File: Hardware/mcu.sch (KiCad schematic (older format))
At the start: 45 parts, among them J3 SWD_programming, J4 Capsense_0, J5 Capsense_1, J6 Capsense_2, J7 Capsense_3, U7 CY8C4246AZI-L445, Y1 Crystal

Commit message: add Cmod cap to microcontroller for capsense operation.
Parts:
- added C?: 2.2nF, symbol C_Small
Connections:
- wire segments 98 -> 79
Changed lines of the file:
@@
 	1050 7350 1350 7350
 Wire Wire Line
-	1850 2150 2050 2150
-Wire Wire Line
-	2050 2150 2150 2150
+	1850 2150 2150 2150
 Wire Wire Line
 	1850 2250 2150 2250
@@
 	2150 2350 1850 2350
 Wire Wire Line
-	1500 4400 1500 4500
-Wire Wire Line
-	1500 4500 1500 4800
-Wire Wire Line
-	1500 4800 1500 4850
+	1500 4400 1500 4850
 Wire Wire Line
 	1500 4400 2150 4400
 Wire Wire Line
-	2000 4500 2000 4800
-Wire Wire Line
-	2000 4800 2000 4850
-Wire Wire Line
-	1900 4500 2000 4500
-Wire Wire Line
-	2000 4500 2150 4500
+	2000 4500 2000 4850
+Wire Wire Line
+	1900 4500 2150 4500
 Connection ~ 2000 4500
 Wire Wire Line
@@
 	2100 3950 2150 3950
 Wire Wire Line
-	1700 3050 1800 3050
-Wire Wire Line
-	1800 3050 1900 3050
-Wire Wire Line
-	1900 3050 2000 3050
+	1700 3050 2000 3050
 Connection ~ 1800 3050
 Wire Wire Line
-	1700 3250 1800 3250
-Wire Wire Line
-	1800 3250 1900 3250
-Wire Wire Line
-	1900 3250 2150 3250
+	1700 3250 2150 3250
 Connection ~ 1800 3250
 $Comp
@@
 $EndComp
 Wire Wire Line
-	1700 4100 1800 4100
-Wire Wire Line
-	1800 4100 1900 4100
-Wire Wire Line
-	1900 4100 2000 4100
+	1700 4100 2000 4100
 Connection ~ 1800 4100
 Wire Wire Line
-	1700 3900 1800 3900
-Wire Wire Line
-	1800 3900 1900 3900
-Wire Wire Line
-	1900 3900 1950 3900
+	1700 3900 1950 3900
 Connection ~ 1800 3900
 Wire Wire Line
@@
 Connection ~ 1250 3950
 Wire Wire Line
-	1050 3200 1150 3200
-Wire Wire Line
-	1150 3200 1250 3200
-Wire Wire Line
-	1250 3200 1550 3200
-Wire Wire Line
-	1050 3400 1150 3400
-Wire Wire Line
-	1150 3400 1250 3400
-Wire Wire Line
-	1250 3400 1400 3400
+	1050 3200 1550 3200
+Wire Wire Line
+	1050 3400 1400 3400
 Wire Wire Line
 	1550 3200 1550 3350
@@
 	2150 3450 1550 3450
 Wire Wire Line
-	1550 3450 1550 3750
-Wire Wire Line
-	1550 3750 1250 3750
-Wire Wire Line
-	1250 3750 1150 3750
-Wire Wire Line
-	1150 3750 1050 3750
+	1550 3750 1550 3450
+Wire Wire Line
+	1050 3750 1550 3750
 Wire Wire Line
 	1400 3400 1400 3550
@@
 	2150 3650 1600 3650
 Wire Wire Line
-	1600 3650 1600 3950
-Wire Wire Line
-	1600 3950 1250 3950
-Wire Wire Line
-	1250 3950 1150 3950
-Wire Wire Line
-	1150 3950 1050 3950
+	1600 3950 1600 3650
+Wire Wire Line
+	1050 3950 1600 3950
 $Comp
 L Conn_01x01 J4
@@
 Wire Wire Line
 	4950 1200 5150 1200
+$Comp
+L C_Small C?
+U 1 1 5C5349C7
+P 5400 4550
+F 0 "C?" H 5410 4620 50  0000 L CNN
+F 1 "2.2nF" H 5410 4470 50  0000 L CNN
+F 2 "" H 5400 4550 50  0001 C CNN
+F 3 "" H 5400 4550 50  0001 C CNN
+	1    5400 4550
+	1    0    0    -1
+$EndComp
+$Comp
+L GNDD #PWR?
+U 1 1 5C534CC8
+P 5400 4650
+F 0 "#PWR?" H 5400 4400 50  0001 C CNN
+F 1 "GNDD" H 5400 4525 50  0000 C CNN
+F 2 "" H 5400 4650 50  0001 C CNN
+F 3 "" H 5400 4650 50  0001 C CNN
+	1    5400 4650
+	-1   0    0    -1
+$EndComp
+Wire Wire Line
+	5400 4450 5400 4400
+Wire Wire Line
+	5400 4400 4950 4400
 $EndSCHEMATC

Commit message: change 3.3V to 5V, fix LFO biasing, LPF, JFET bias trim pots.
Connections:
- net labels added: +5V
- net labels removed: +3.3V
- wire segments 79 -> 100

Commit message: add quantization switches
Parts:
- added R? (x4): R, digikey-footprints:0805, symbol R
- added SW? (x4): SW_SPST, symbol SW_SPST
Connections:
- net +5V: now also R?.2, R?.2, R?.2, R?.2
- net GNDD: now also SW?.1 (A), SW?.1 (A), SW?.1 (A), SW?.1 (A)
- net osc4_quant: now reaches U7.58 (P1.0)
- net osc4_quant: now also R?.1, SW?.2 (B)
- net osc3_quant: now reaches U7.59 (P1.1)
- net osc3_quant: now also R?.1, SW?.2 (B)
- net osc2_quant: now reaches U7.60 (P1.2)
- net osc2_quant: now also R?.1, SW?.2 (B)
- net osc1_quant: now reaches U7.61 (P1.3)
- net osc1_quant: now also R?.1, SW?.2 (B)
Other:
- note added: "MCU pins have resistive pull \nup as an option, so probably \nleave these resistors unloaded."

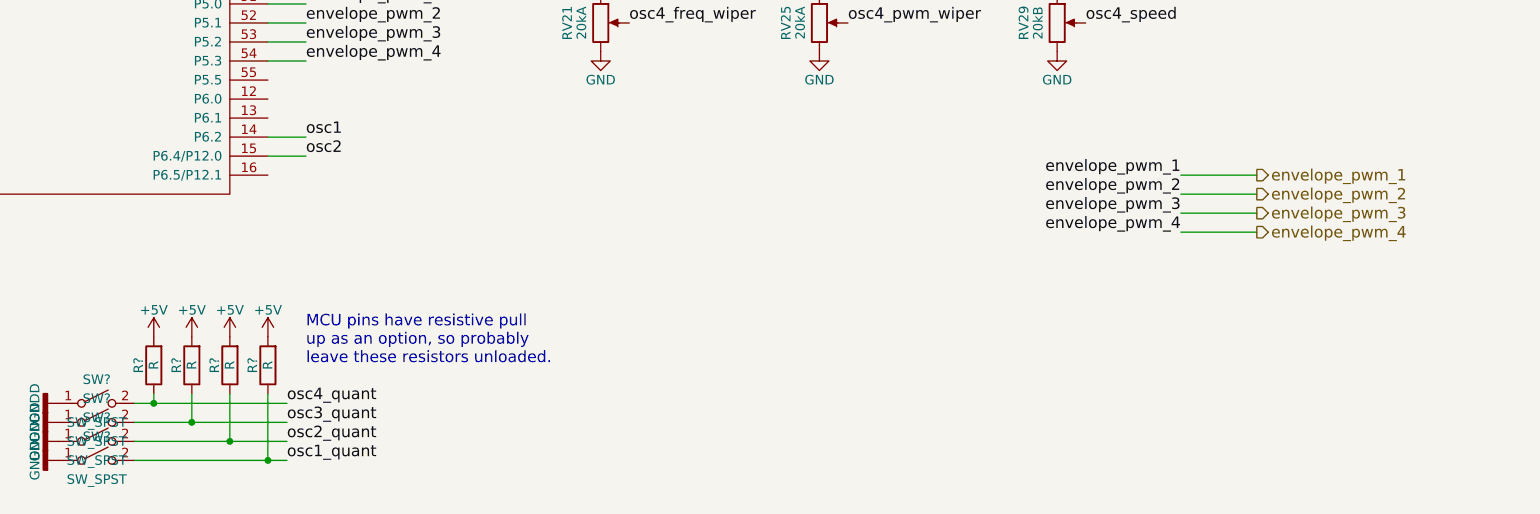
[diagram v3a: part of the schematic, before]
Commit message: add LPF to envelope PWM outputs
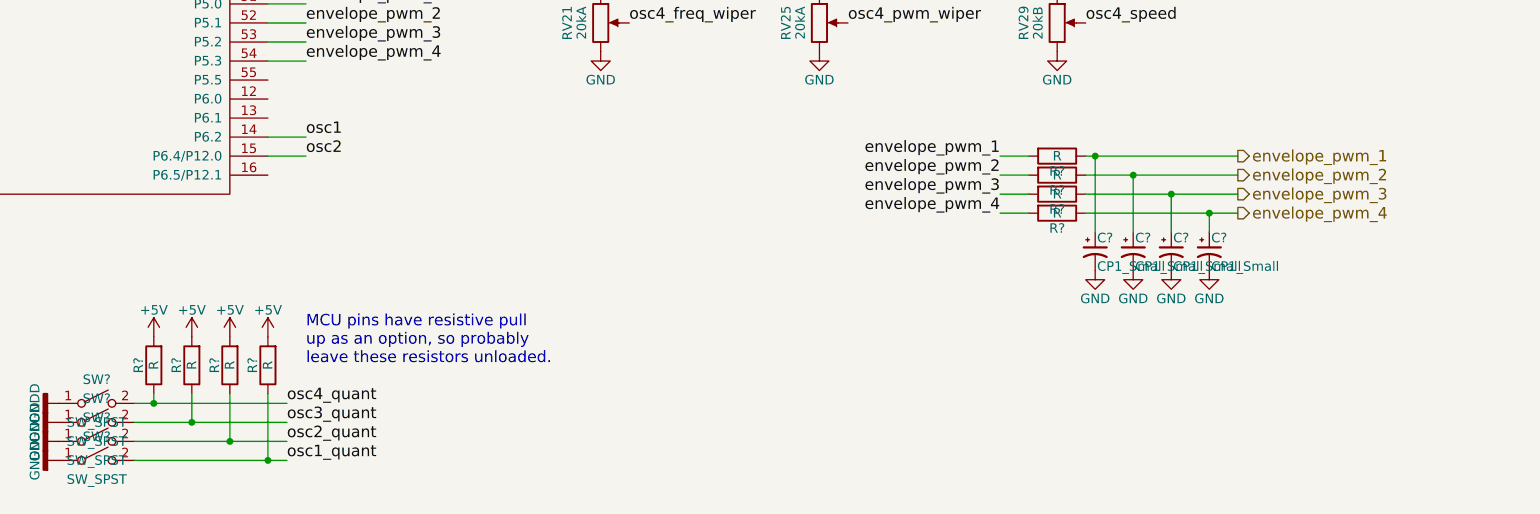
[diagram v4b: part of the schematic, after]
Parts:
- added C? (x4): CP1_Small, symbol CP1_Small
- added R? (x4): R, digikey-footprints:0805, symbol R
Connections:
- net GND: now also C?.2, C?.2, C?.2, C?.2
- net envelope_pwm_1: now also C?.1, R?.1, R?.2
- net envelope_pwm_2: now also C?.1, R?.1, R?.2
- net envelope_pwm_3: now also C?.1, R?.1, R?.2
- net envelope_pwm_4: now also C?.1, R?.1, R?.2

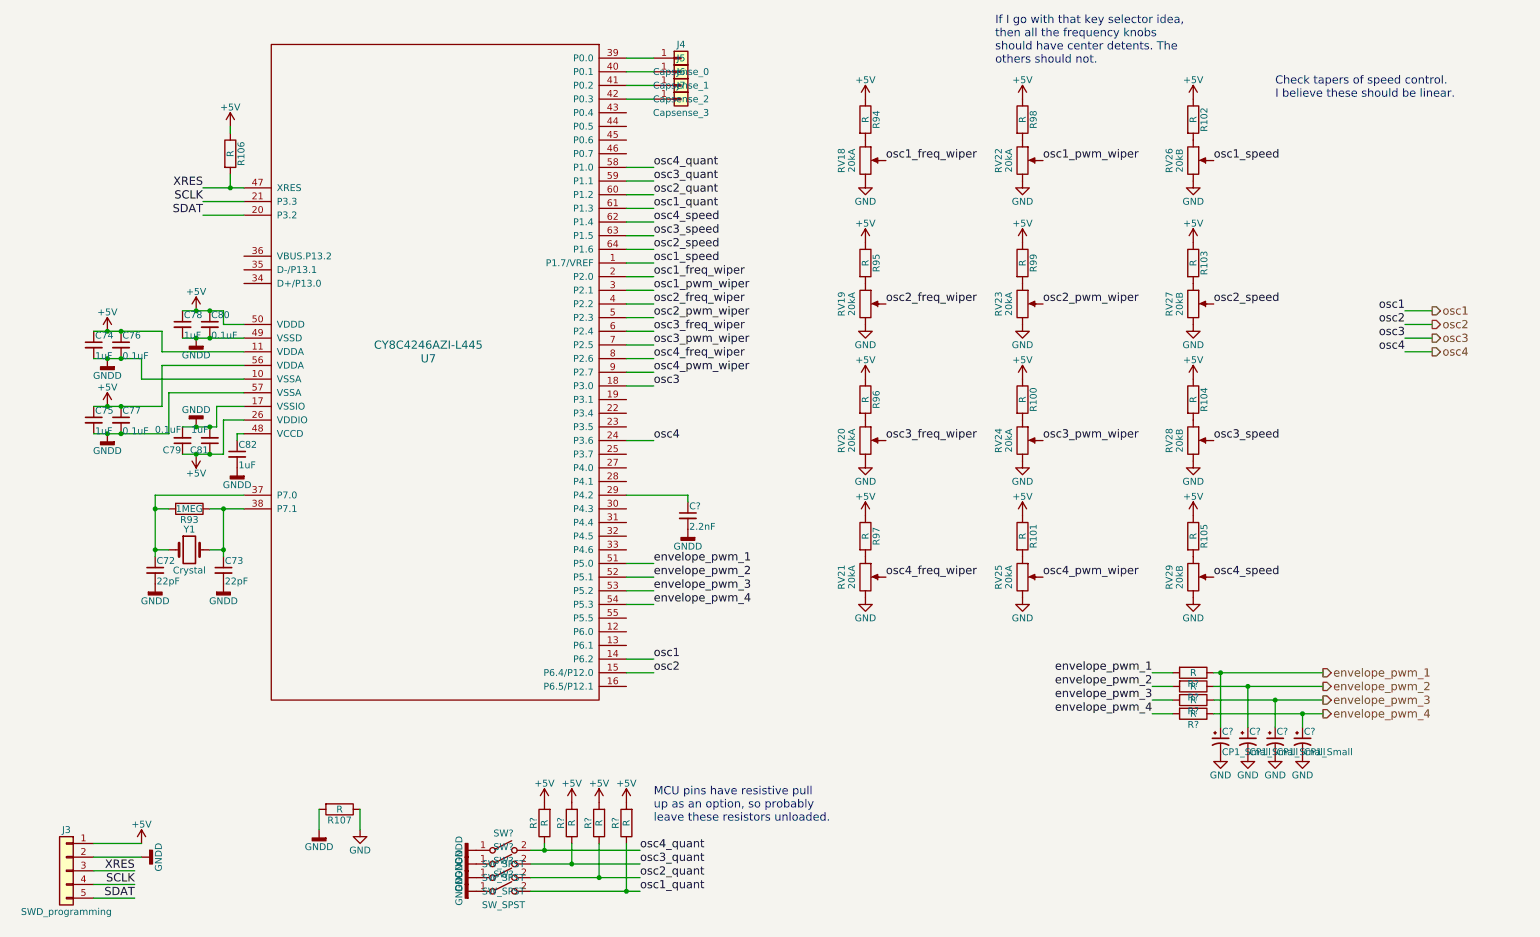
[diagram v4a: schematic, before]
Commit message: add envelope repeat switches
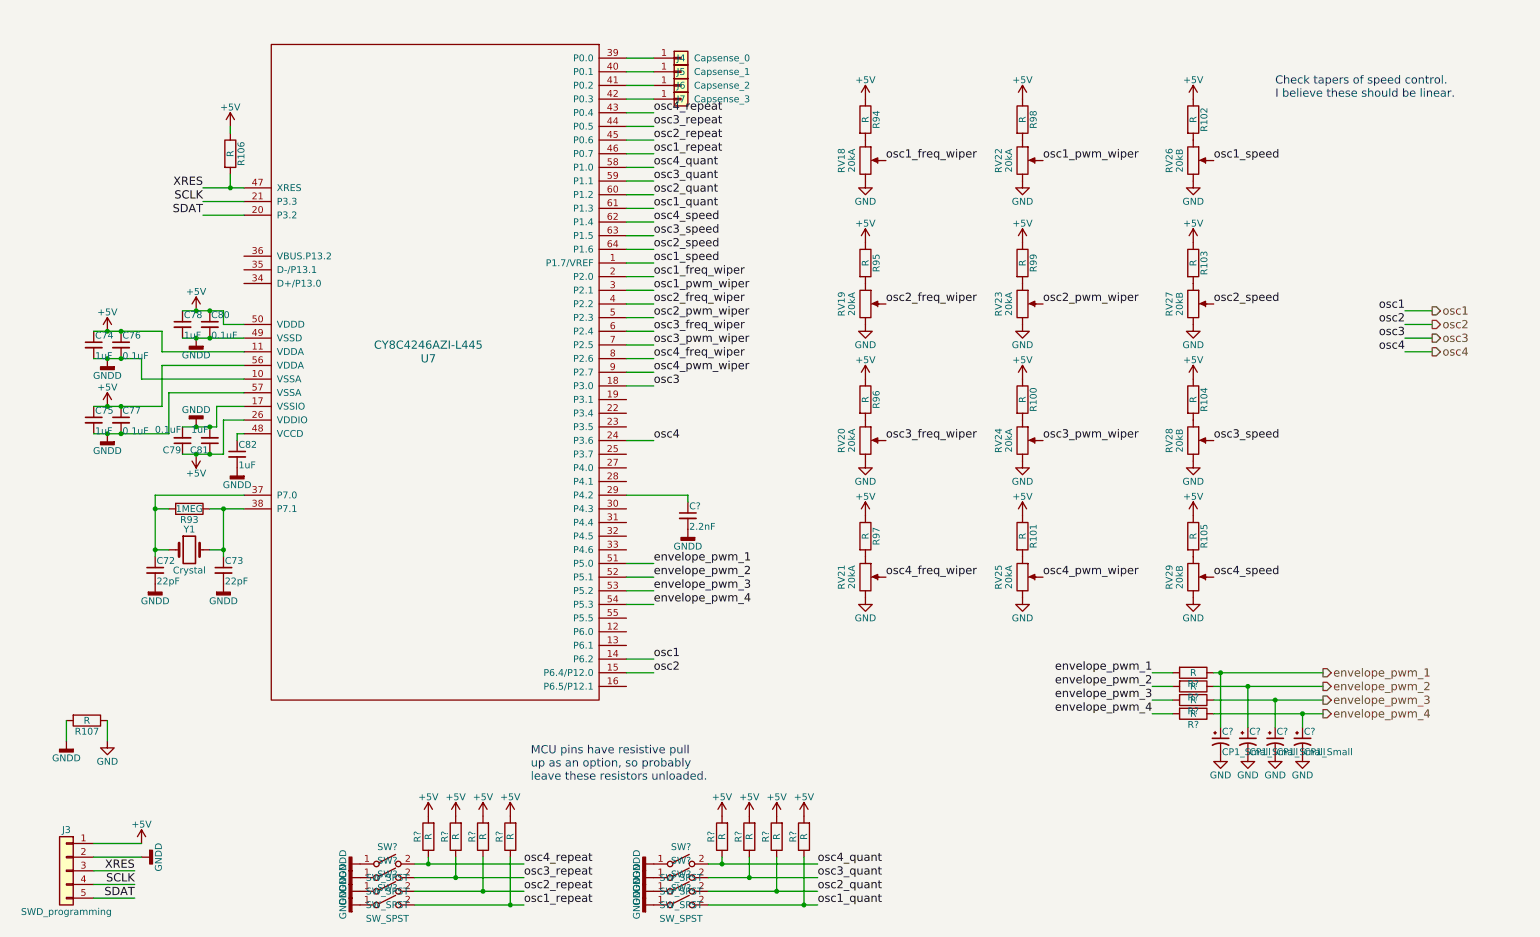
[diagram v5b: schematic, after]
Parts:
- added R? (x4): R, digikey-footprints:0805, symbol R
- added SW? (x4): SW_SPST, symbol SW_SPST
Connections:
- net +5V: now also R?.2, R?.2, R?.2, R?.2
- net GNDD: now also SW?.1 (A), SW?.1 (A), SW?.1 (A), SW?.1 (A)
- net osc4_repeat: now reaches U7.43 (P0.4)
- net osc4_repeat: now also R?.1, SW?.2 (B)
- net osc3_repeat: now reaches U7.44 (P0.5)
- net osc3_repeat: now also R?.1, SW?.2 (B)
- net osc2_repeat: now reaches U7.45 (P0.6)
- net osc2_repeat: now also R?.1, SW?.2 (B)
- net osc1_repeat: now reaches U7.46 (P0.7)
- net osc1_repeat: now also R?.1, SW?.2 (B)
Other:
- note removed: "If I go with that key selector idea, \nthen all the frequency knobs \nshould have center detents. The \nothers should not."
- moved on the sheet: R107, R?, SW?

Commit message: simulate bias voltage buffer. Previous op amp approach couldn't go close enough to the rails.
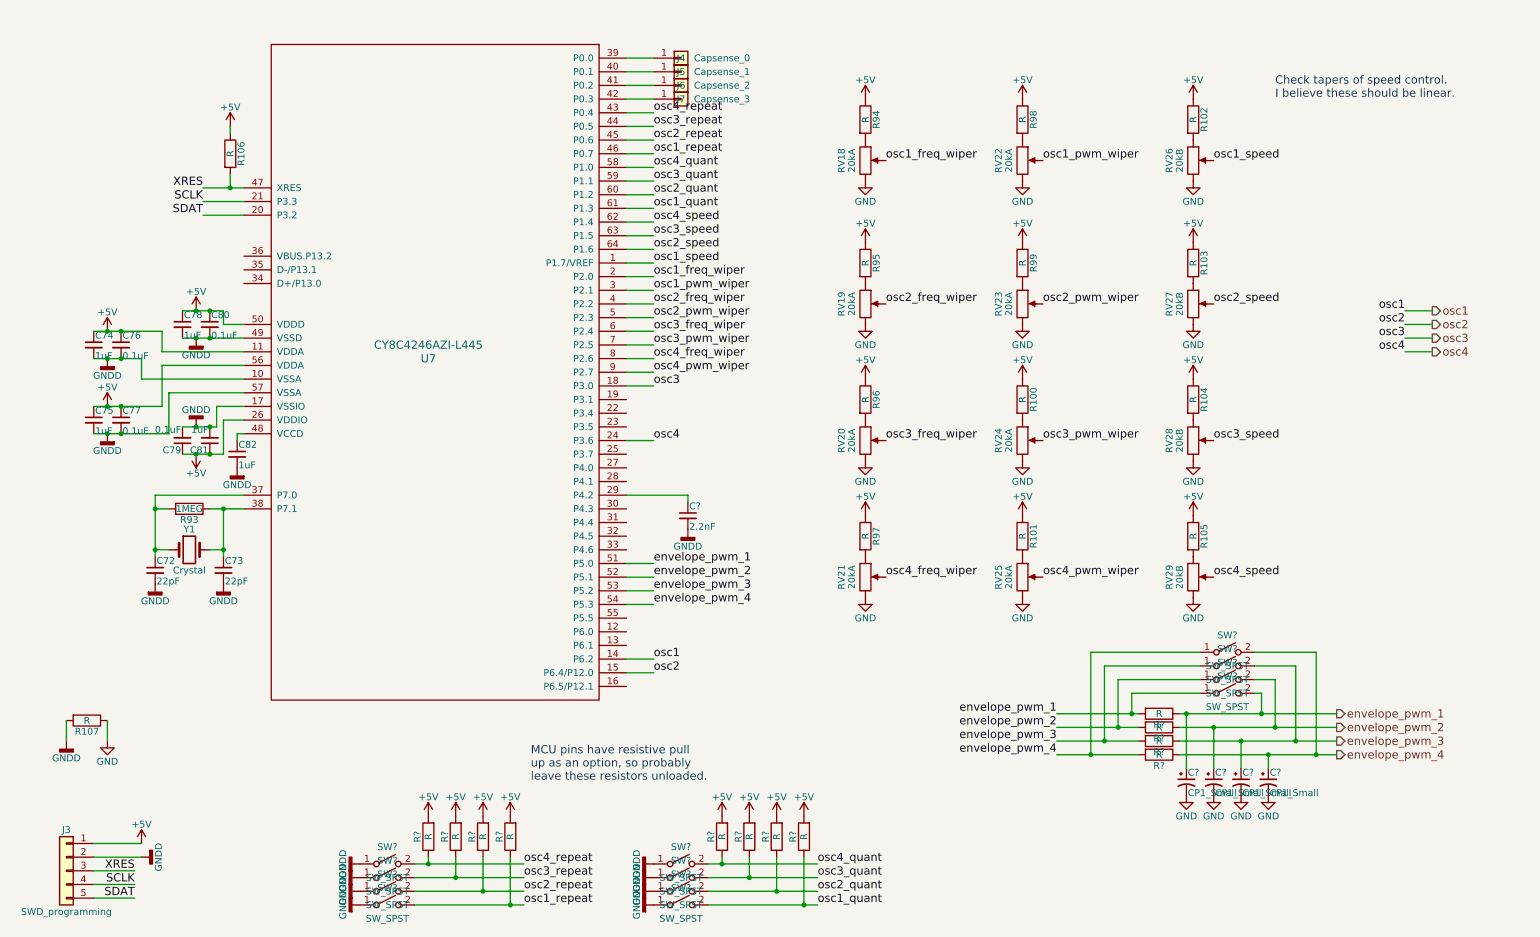
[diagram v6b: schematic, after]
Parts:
- added SW? (x4): SW_SPST, symbol SW_SPST
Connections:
- net envelope_pwm_1: now also SW?.1 (A), SW?.2 (B)
- net envelope_pwm_2: now also SW?.1 (A), SW?.2 (B)
- net envelope_pwm_3: now also SW?.1 (A), SW?.2 (B)
- net envelope_pwm_4: now also SW?.1 (A), SW?.2 (B)
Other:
- moved on the sheet: C?, R?
